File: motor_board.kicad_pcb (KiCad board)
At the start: 2 copper layers, 100 x 100 mm, 44 parts, among them J1 MyRIO_C, J10 ESCON_24-2, J11 Conn_01x02, J12 Conn_01x05, J13 Conn_01x03, J14 BNC, J15 BNC, J2 BNC, J3 BNC, J4 BNC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

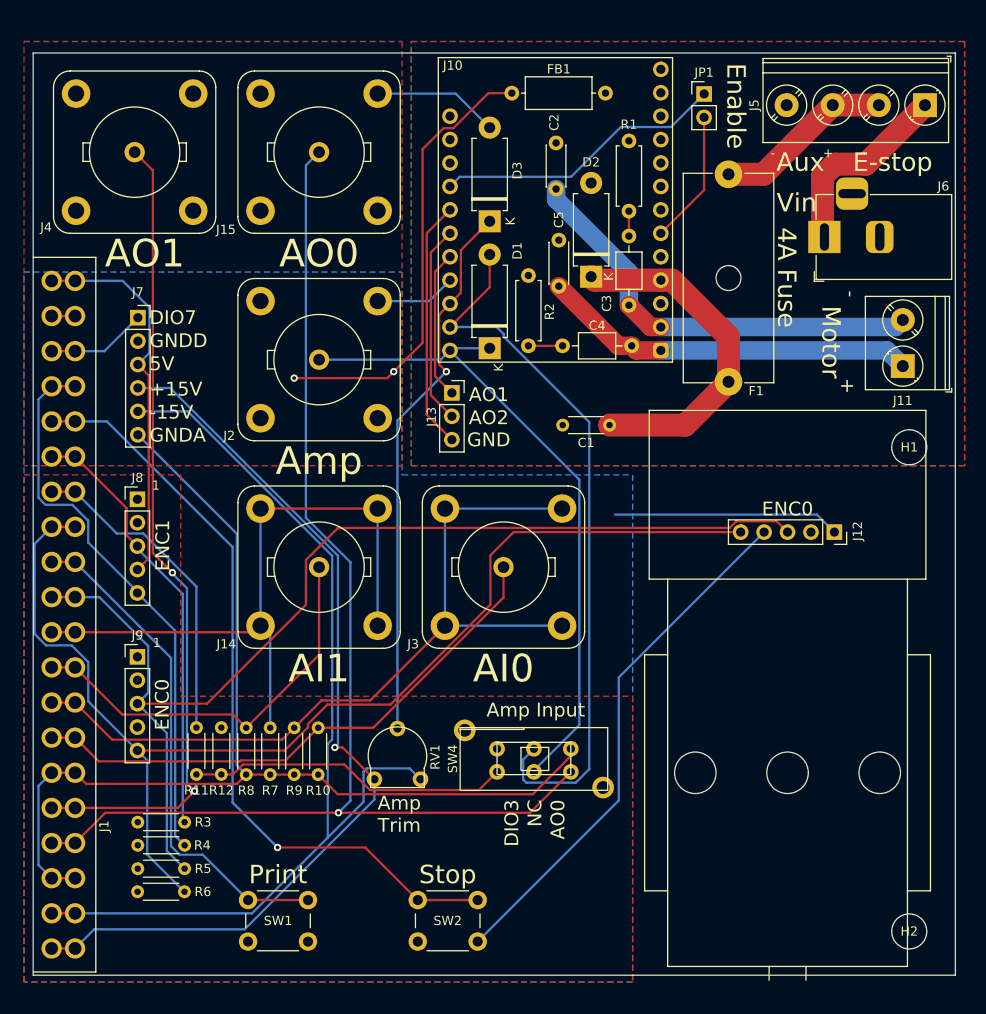
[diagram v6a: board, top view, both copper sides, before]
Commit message: updated the board to use a 10k pot that is hopefully more heat resistant and has longer leads.
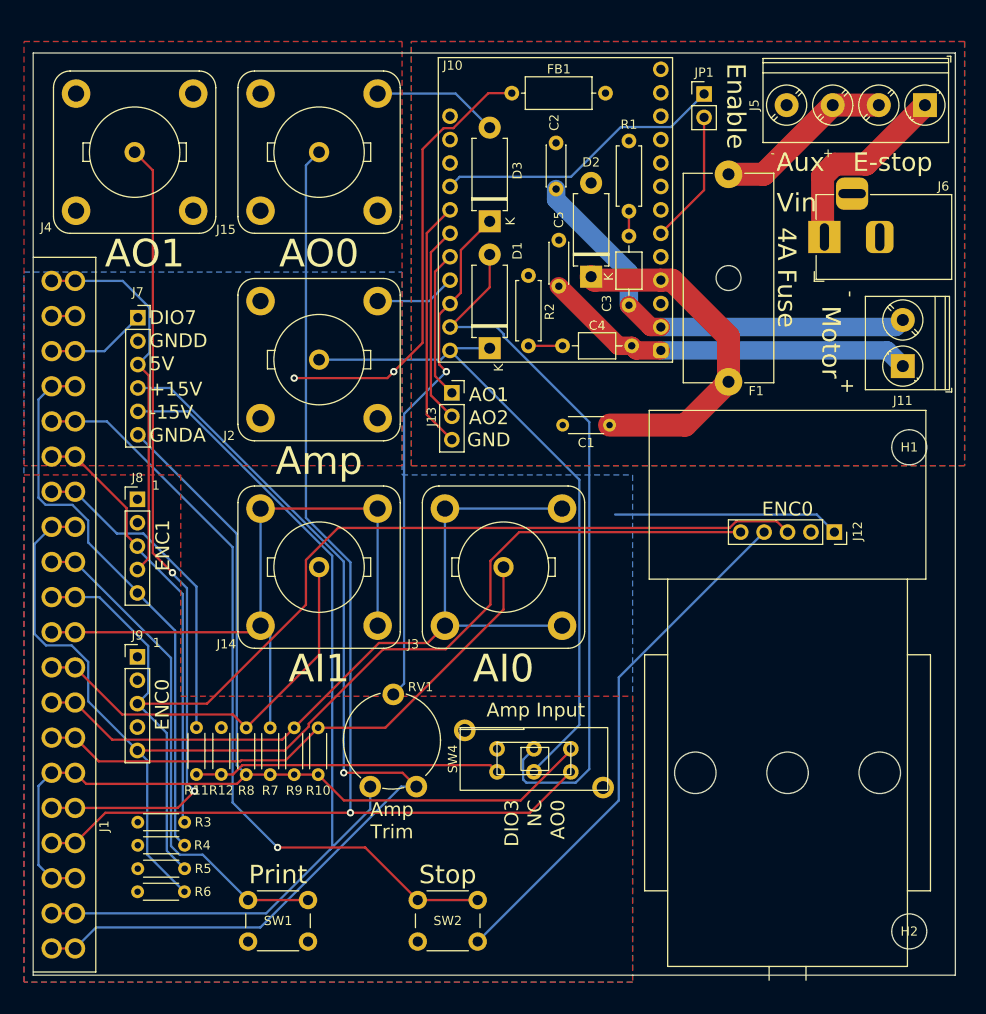
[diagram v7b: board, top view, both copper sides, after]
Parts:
- RV1: value 1k -> 10k; footprint motor_board:CUI PTN06-E Pot -> Potentiometer_THT:Potentiometer_Piher_PT-10-V10_Vertical
- moved RV1 3.88 mm to (79.5, 116.8)
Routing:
- net /+15V: track 99.8 -> 108.3 mm
- net /-15V: track 107.2 -> 101.2 mm
- net Net-(D3-A1): track 59.8 -> 56.3 mm
- net Net-(SW4A-C): track 35.0 -> 33.3 mm
- net Net-(J1-AI0+): track 60.7 -> 61.5 mm
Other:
- board text added: "Designed By: Cameron Devine October 2024"
- board text removed: "Designed By: Cameron Devine August 2024"

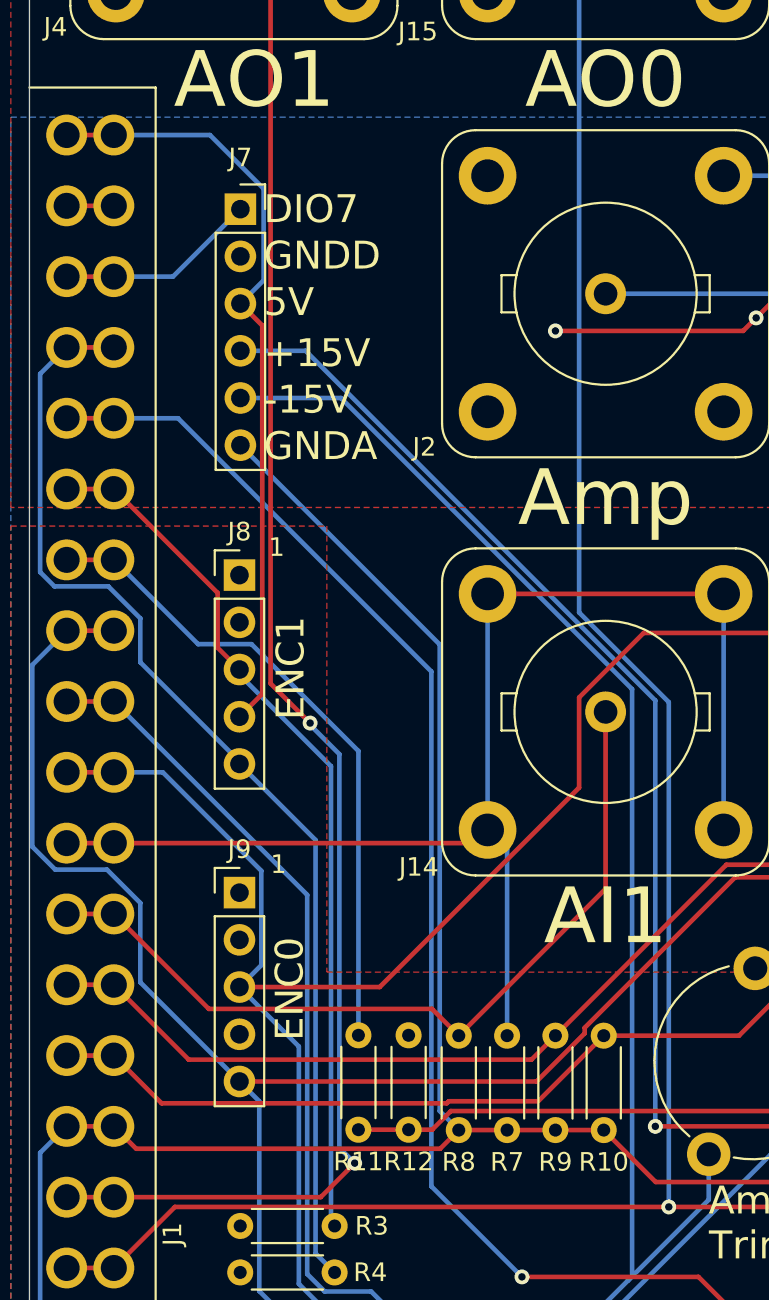
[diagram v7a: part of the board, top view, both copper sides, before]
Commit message: added a resistor divider to get the correct current for lab 4, added DIO3 to the aux header, and changed to a more durable 10 k put to keep from overloading the +/-15 V supply.
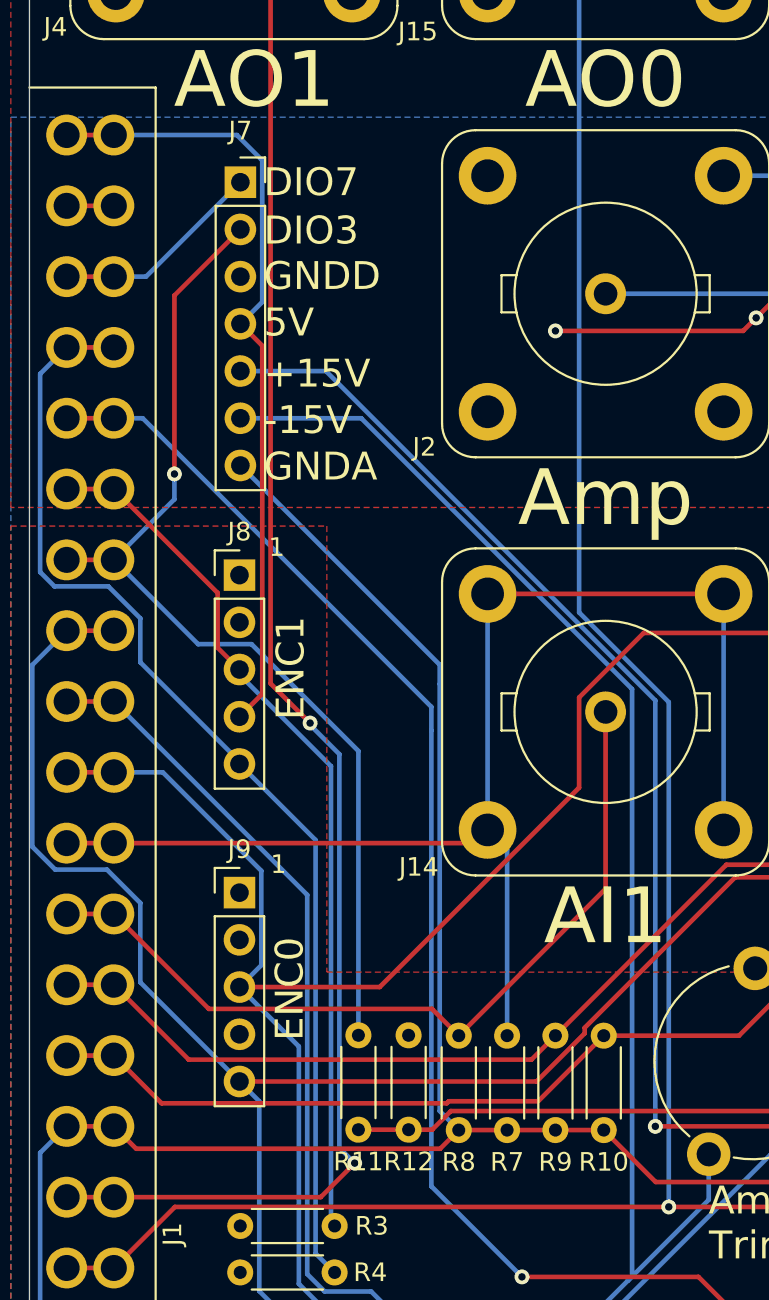
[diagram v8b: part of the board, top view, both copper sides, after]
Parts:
- J7: value Conn_01x06 -> Conn_01x07; footprint Connector_PinSocket_2.54mm:PinSocket_1x06_P2.54mm_Vertical -> Connector_PinSocket_2.54mm:PinSocket_1x07_P2.54mm_Vertical
- R11: value 22k -> 2.7k
- R12: value 8.2k -> 1k
- moved J7 1.45 mm to (49.4, 64.5)
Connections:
- J7 pad 2: GNDD -> Net-(J1-DIO3/PWM0)
- J7 pad 3: Net-(J1-5V) -> GNDD
- J7 pad 4: /+15V -> Net-(J1-5V)
- J7 pad 5: /-15V -> /+15V
- J7 pad 6: GNDA -> /-15V
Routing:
- net Net-(J1-DIO3/PWM0): track 35.8 -> 55.9 mm, vias 0 -> 1
- net Net-(J1-DIO5): track 83.9 -> 82.8 mm
- net GNDA: track 140.4 -> 139.3 mm
- net Net-(J1-5V): track 99.0 -> 99.8 mm
- net Net-(J1-DIO7/PWM1): track 10.9 -> 11.5 mm
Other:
- board text added: "Designed By: Cameron Devine November 2024"
- board text removed: "Designed By: Cameron Devine October 2024"
